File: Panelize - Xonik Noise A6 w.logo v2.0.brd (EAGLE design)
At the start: 29.8 x 26 mm, 39 parts, among them IC1 TL074D, T1 NOISE-2N3904

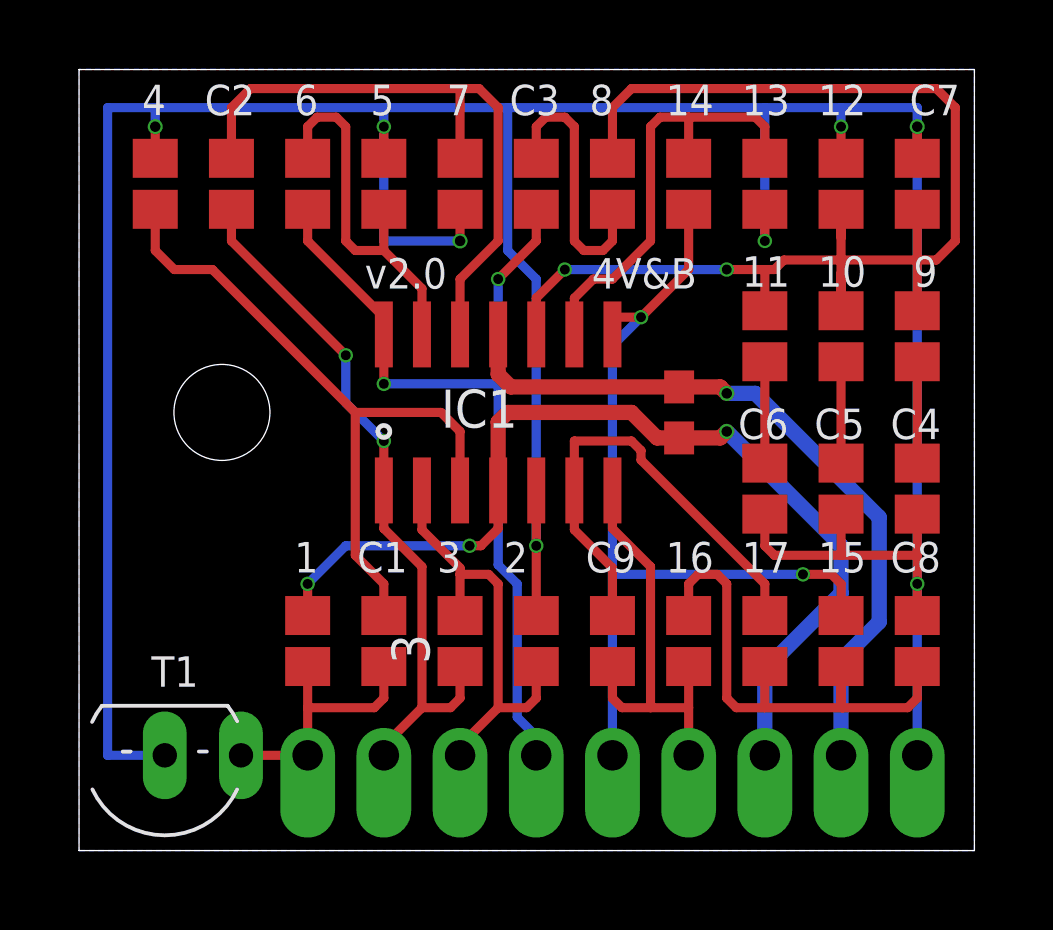
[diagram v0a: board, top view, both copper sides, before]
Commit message: Changed recommended external trimmer for 50k to 100k to be able to reach a high enough amplitude
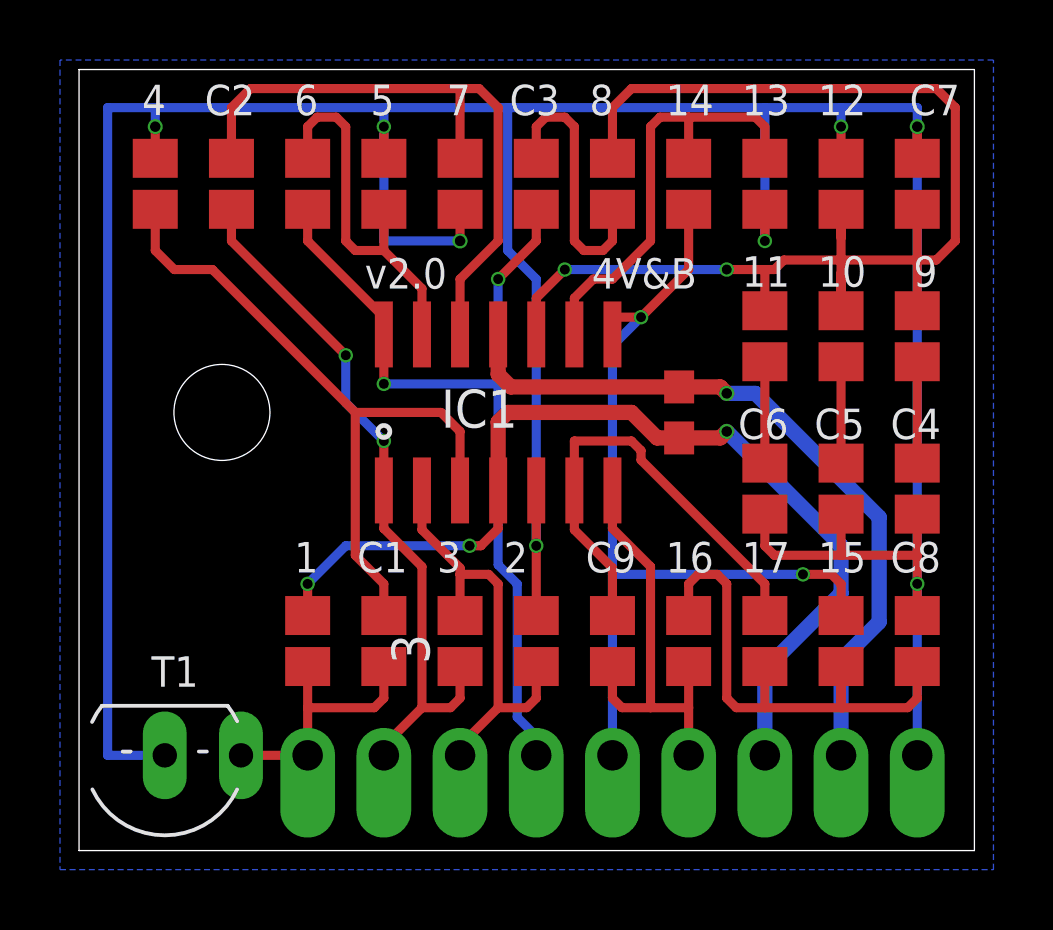
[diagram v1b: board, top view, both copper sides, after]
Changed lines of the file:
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@@
 <layer number="23" name="tOrigins" color="15" fill="1" visible="yes" active="yes"/>
 <layer number="24" name="bOrigins" color="15" fill="1" visible="yes" active="yes"/>
-<layer number="25" name="tNames" color="7" fill="1" visible="no" active="yes"/>
-<layer number="26" name="bNames" color="7" fill="1" visible="no" active="yes"/>
+<layer number="25" name="tNames" color="7" fill="1" visible="yes" active="yes"/>
+<layer number="26" name="bNames" color="7" fill="1" visible="yes" active="yes"/>
 <layer number="27" name="tValues" color="7" fill="1" visible="no" active="yes"/>
 <layer number="28" name="bValues" color="7" fill="1" visible="no" active="yes"/>
@@
 <layer number="123" name="tTestmark" color="7" fill="1" visible="no" active="yes"/>
 <layer number="124" name="bTestmark" color="7" fill="1" visible="no" active="yes"/>
-<layer number="125" name="_tNames" color="14" fill="1" visible="yes" active="yes"/>
+<layer number="125" name="_tNames" color="14" fill="1" visible="no" active="yes"/>
 <layer number="126" name="BIFRNTMAT" color="7" fill="1" visible="no" active="yes"/>
 <layer number="127" name="Info2" color="7" fill="1" visible="no" active="yes"/>
@@
 <wire x1="25.4" y1="11.215" x2="25.4" y2="9.8425" width="0.3048" layer="1"/>
 <polygon width="0.3048" layer="16">
-<vertex x="0" y="26.035"/>
-<vertex x="0" y="0"/>
-<vertex x="29.845" y="0"/>
-<vertex x="29.845" y="26.035"/>
+<vertex x="-0.635" y="26.3525"/>
+<vertex x="-0.635" y="-0.635"/>
+<vertex x="30.48" y="-0.635"/>
+<vertex x="30.48" y="26.3525"/>
 </polygon>
 </signal>
